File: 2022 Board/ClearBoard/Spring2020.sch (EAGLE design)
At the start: 20 parts, among them U1 TB67H401FTG(O,EL), U2 ABX00012, U3 V36SE05010NRFA

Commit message: Almost done with place and route
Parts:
- removed C1: ECA1CM101I, SnapEDA Library:ECA1CM101I
- removed U3: V36SE05010NRFA, SnapEDA Library:V36SE05010NRFA
- added PS1: NID100-5, SnapEDA Library:NID100-5
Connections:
- removed net BKGND: BIKE-PWR-1.KL, C15.2, C19.2, C3.2, GND-JUMPER.2, REAR-MOTOR.1, U$2.GND2, U$7.GND2, U1.GND_3, U3.-VIN
- removed net N$1: U3.-SENSE
- net 5V: now also PS1.+VOUT; no longer C1.P, U3.+SENSE, U3.+VOUT
- net BKPWR: now also PS1.+VIN; no longer U3.+VIN
- net GND: now also BIKE-PWR-1.KL, C15.2, C19.2, C3.2, GND-JUMPER.2, PS1.COM, REAR-MOTOR.1, U$2.GND2, U$7.GND2, U1.GND_3; no longer C1.N, U3.-VOUT
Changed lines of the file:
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@@
 <part name="U2" library="SnapEDA Library" deviceset="ABX00012" device=""/>
 <part name="PWM" library="rcl" library_urn="urn:adsk.eagle:library:334" deviceset="R-US_" device="0204/2V" package3d_urn="urn:adsk.eagle:package:23495/1" value="68000"/>
-<part name="U3" library="SnapEDA Library" deviceset="V36SE05010NRFA" device=""/>
-<part name="C1" library="SnapEDA Library" deviceset="ECA1CM101I" device=""/>
 <part name="U$3" library="Spring2016Optoisolator" deviceset="IL-711" device=""/>
 <part name="C2" library="resistor" deviceset="C-US" device="025-050X050"/>
@@
 <part name="U$2" library="Spring2016Optoisolator" deviceset="IL-712" device=""/>
 <part name="U1" library="Test" deviceset="TB67H401FTG(O,EL)" device=""/>
+<part name="PS1" library="SnapEDA Library" deviceset="NID100-5" device=""/>
 </parts>
 <sheets>
@@
 <attribute name="VALUE" x="166.37" y="155.702" size="1.778" layer="96" rot="R180"/>
 </instance>
-<instance part="U3" gate="G$1" x="294.64" y="147.32" smashed="yes">
-<attribute name="NAME" x="281.94" y="158.75" size="1.778" layer="95"/>
-<attribute name="VALUE" x="281.94" y="134.62" size="1.778" layer="96"/>
-</instance>
-<instance part="C1" gate="G$1" x="325.12" y="157.48" smashed="yes" rot="R270">
-<attribute name="NAME" x="328.93" y="160.02" size="1.778" layer="95" rot="R270"/>
-<attribute name="VALUE" x="320.04" y="160.02" size="1.778" layer="96" rot="R270"/>
-</instance>
 <instance part="U$3" gate="G$1" x="337.82" y="45.72" smashed="yes" rot="R180"/>
 <instance part="C2" gate="G$1" x="88.9" y="124.46" smashed="yes" rot="R270">
@@
 <attribute name="NAME" x="188.3156" y="98.0186" size="2.0828" layer="95" ratio="6" rot="SR0"/>
 <attribute name="VALUE" x="187.6806" y="95.4786" size="2.0828" layer="96" ratio="6" rot="SR0"/>
+</instance>
+<instance part="PS1" gate="G$1" x="294.64" y="177.8" smashed="yes">
+<attribute name="NAME" x="279.4" y="186.182" size="1.778" layer="95"/>
+<attribute name="VALUE" x="279.4" y="167.64" size="1.778" layer="96"/>
 </instance>
 </instances>
@@
 </segment>
 <segment>
-<pinref part="C1" gate="G$1" pin="N"/>
-<pinref part="U3" gate="G$1" pin="-VOUT"/>
-<wire x1="325.12" y1="152.4" x2="312.42" y2="152.4" width="0.1524" layer="91"/>
-<label x="312.42" y="152.4" size="1.778" layer="95"/>
-</segment>
-<segment>
 <wire x1="93.98" y1="109.22" x2="83.82" y2="109.22" width="0.1524" layer="91"/>
 <label x="93.98" y="109.22" size="1.778" layer="95" rot="R180"/>
@@
 <wire x1="83.82" y1="124.46" x2="78.74" y2="124.46" width="0.1524" layer="91"/>
 <label x="78.74" y="124.46" size="1.778" layer="95"/>
+</segment>
+<segment>
+<pinref part="PS1" gate="G$1" pin="COM"/>
+<wire x1="314.96" y1="172.72" x2="325.12" y2="172.72" width="0.1524" layer="91"/>
+<label x="317.5" y="172.72" size="1.778" layer="95"/>
+</segment>
+<segment>
+<pinref part="BIKE-PWR" gate="-1" pin="KL"/>
+<wire x1="294.64" y1="48.26" x2="292.1" y2="48.26" width="0.1524" layer="91"/>
+<label x="294.64" y="48.26" size="1.778" layer="95"/>
+</segment>
+<segment>
+<pinref part="GND-JUMPER" gate="A" pin="2"/>
+<wire x1="289.56" y1="25.4" x2="294.64" y2="25.4" width="0.1524" layer="91"/>
+<label x="292.1" y="25.4" size="1.778" layer="95"/>
+</segment>
+<segment>
+<wire x1="170.18" y1="53.34" x2="160.02" y2="53.34" width="0.1524" layer="91"/>
+<label x="160.02" y="53.34" size="1.778" layer="95"/>
+<pinref part="U1" gate="A" pin="GND_3"/>
+</segment>
+<segment>
+<pinref part="REAR-MOTOR" gate="1" pin="1"/>
+<wire x1="195.58" y1="154.94" x2="187.96" y2="154.94" width="0.1524" layer="91"/>
+<label x="195.58" y="154.94" size="1.778" layer="95" rot="R180"/>
+</segment>
+<segment>
+<wire x1="129.54" y1="142.24" x2="134.62" y2="142.24" width="0.1524" layer="91"/>
+<label x="129.54" y="142.24" size="1.778" layer="95"/>
+<pinref part="U$7" gate="G$1" pin="GND2"/>
+</segment>
+<segment>
+<pinref part="C19" gate="G$1" pin="2"/>
+<wire x1="147.32" y1="157.48" x2="149.86" y2="157.48" width="0.1524" layer="91"/>
+<label x="147.32" y="157.48" size="1.778" layer="95"/>
+</segment>
+<segment>
+<pinref part="C15" gate="G$1" pin="2"/>
+<wire x1="167.64" y1="142.24" x2="167.64" y2="139.7" width="0.1524" layer="91"/>
+<label x="167.64" y="142.24" size="1.778" layer="95"/>
+</segment>
+<segment>
+<wire x1="127" y1="109.22" x2="132.08" y2="109.22" width="0.1524" layer="91"/>
+<label x="127" y="109.22" size="1.778" layer="95"/>
+<pinref part="U$2" gate="G$1" pin="GND2"/>
+</segment>
+<segment>
+<pinref part="C3" gate="G$1" pin="2"/>
+<wire x1="144.78" y1="124.46" x2="149.86" y2="124.46" width="0.1524" layer="91"/>
+<label x="144.78" y="124.46" size="1.778" layer="95"/>
 </segment>
 </net>
@@
 </segment>
 </net>
-<net name="BKGND" class="0">
-<segment>
-<pinref part="BIKE-PWR" gate="-1" pin="KL"/>
-<wire x1="294.64" y1="48.26" x2="292.1" y2="48.26" width="0.1524" layer="91"/>
-<label x="294.64" y="48.26" size="1.778" layer="95"/>
-</segment>
-<segment>
-<pinref part="GND-JUMPER" gate="A" pin="2"/>
-<wire x1="289.56" y1="25.4" x2="294.64" y2="25.4" width="0.1524" layer="91"/>
-<label x="292.1" y="25.4" size="1.778" layer="95"/>
-</segment>
-<segment>
-<wire x1="170.18" y1="53.34" x2="160.02" y2="53.34" width="0.1524" layer="91"/>
-<label x="160.02" y="53.34" size="1.778" layer="95"/>
-<pinref part="U1" gate="A" pin="GND_3"/>
-</segment>
-<segment>
-<pinref part="REAR-MOTOR" gate="1" pin="1"/>
-<wire x1="195.58" y1="154.94" x2="187.96" y2="154.94" width="0.1524" layer="91"/>
-<label x="195.58" y="154.94" size="1.778" layer="95" rot="R180"/>
-</segment>
-<segment>
-<wire x1="129.54" y1="142.24" x2="134.62" y2="142.24" width="0.1524" layer="91"/>
-<label x="129.54" y="142.24" size="1.778" layer="95"/>
-<pinref part="U$7" gate="G$1" pin="GND2"/>
-</segment>
-<segment>
-<pinref part="C19" gate="G$1" pin="2"/>
-<wire x1="147.32" y1="157.48" x2="149.86" y2="157.48" width="0.1524" layer="91"/>
-<label x="147.32" y="157.48" size="1.778" layer="95"/>
-</segment>
-<segment>
-<pinref part="C15" gate="G$1" pin="2"/>
-<wire x1="167.64" y1="142.24" x2="167.64" y2="139.7" width="0.1524" layer="91"/>
-<label x="167.64" y="142.24" size="1.778" layer="95"/>
-</segment>
-<segment>
-<pinref part="U3" gate="G$1" pin="-VIN"/>
-<wire x1="266.7" y1="152.4" x2="276.86" y2="152.4" width="0.1524" layer="91"/>
-<label x="266.7" y="152.4" size="1.778" layer="95"/>
-</segment>
-<segment>
-<wire x1="127" y1="109.22" x2="132.08" y2="109.22" width="0.1524" layer="91"/>
-<label x="127" y="109.22" size="1.778" layer="95"/>
-<pinref part="U$2" gate="G$1" pin="GND2"/>
-</segment>
-<segment>
-<pinref part="C3" gate="G$1" pin="2"/>
-<wire x1="144.78" y1="124.46" x2="149.86" y2="124.46" width="0.1524" layer="91"/>
-<label x="144.78" y="124.46" size="1.778" layer="95"/>
-</segment>
-</net>
 <net name="CH5" class="0">
 <segment>
@@
 </segment>
 <segment>
-<pinref part="U3" gate="G$1" pin="+SENSE"/>
-<wire x1="274.32" y1="147.32" x2="276.86" y2="147.32" width="0.1524" layer="91"/>
-<label x="274.32" y="147.32" size="1.778" layer="95"/>
-</segment>
-<segment>
-<pinref part="U3" gate="G$1" pin="+VOUT"/>
-<wire x1="312.42" y1="154.94" x2="317.5" y2="154.94" width="0.1524" layer="91"/>
-<label x="312.42" y="154.94" size="1.778" layer="95"/>
-<wire x1="317.5" y1="154.94" x2="317.5" y2="160.02" width="0.1524" layer="91"/>
-<pinref part="C1" gate="G$1" pin="P"/>
-<wire x1="317.5" y1="160.02" x2="325.12" y2="160.02" width="0.1524" layer="91"/>
-</segment>
-<segment>
 <label x="129.54" y="124.46" size="1.778" layer="95"/>
 <wire x1="127" y1="124.46" x2="137.16" y2="124.46" width="0.1524" layer="91"/>
@@
 <pinref part="U$2" gate="G$1" pin="VDD2"/>
 </segment>
+<segment>
+<pinref part="PS1" gate="G$1" pin="+VOUT"/>
+<wire x1="314.96" y1="182.88" x2="325.12" y2="182.88" width="0.1524" layer="91"/>
+<label x="317.5" y="182.88" size="1.778" layer="95"/>
+</segment>
 </net>
 <net name="BKPWR" class="0">
@@
 </segment>
 <segment>
-<pinref part="U3" gate="G$1" pin="+VIN"/>
-<label x="266.7" y="154.94" size="1.778" layer="95"/>
-<wire x1="276.86" y1="154.94" x2="266.7" y2="154.94" width="0.1524" layer="91"/>
+<wire x1="274.32" y1="182.88" x2="264.16" y2="182.88" width="0.1524" layer="91"/>
+<pinref part="PS1" gate="G$1" pin="+VIN"/>
+<label x="264.16" y="182.88" size="1.778" layer="95"/>
 </segment>
 </net>
@@
 </segment>
 </net>
-<net name="N$1" class="0">
-<segment>
-<pinref part="U3" gate="G$1" pin="-SENSE"/>
-<wire x1="276.86" y1="144.78" x2="271.78" y2="144.78" width="0.1524" layer="91"/>
-</segment>
-</net>

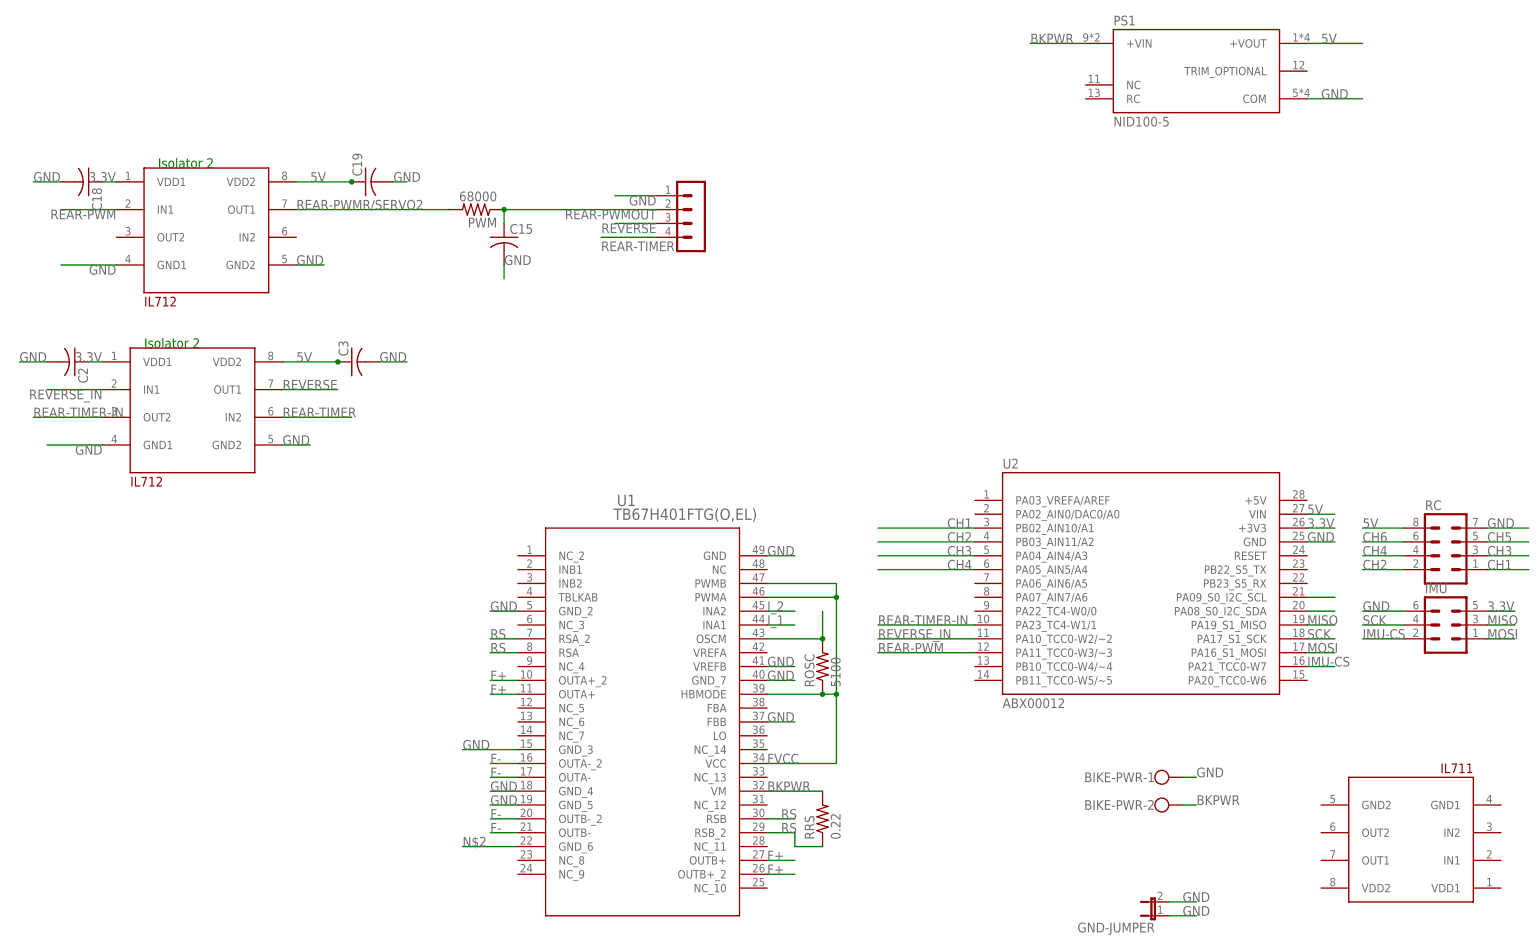
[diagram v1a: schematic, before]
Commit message: Finished front motor attachments
Also positioned things in board
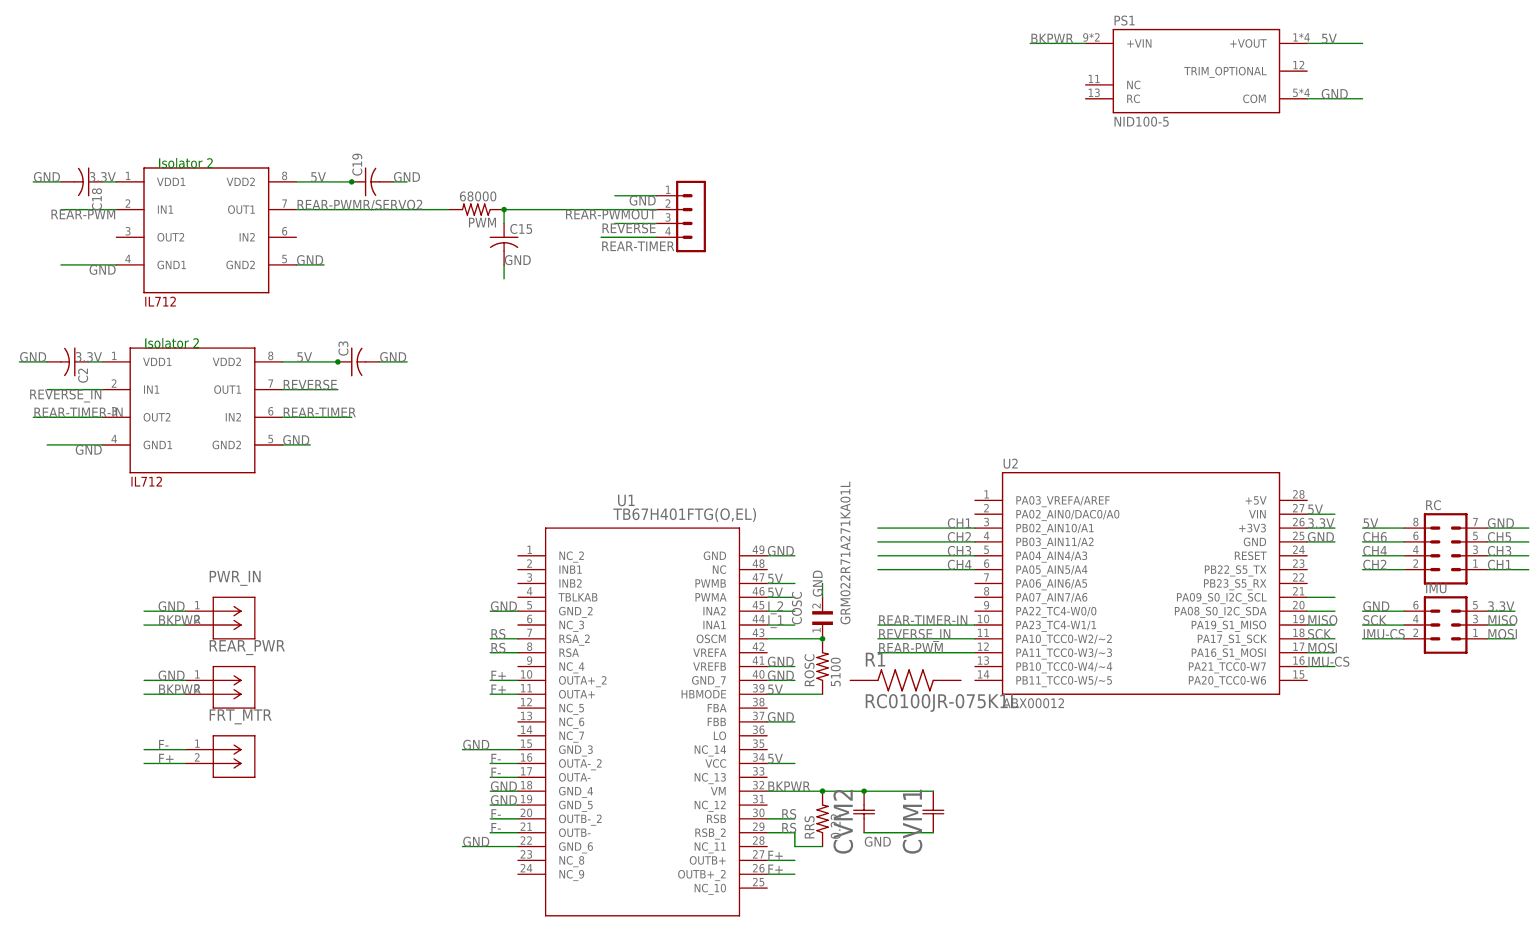
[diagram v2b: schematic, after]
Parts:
- removed BIKE-PWR: (no value), con-wago-500:W237-102
- removed GND-JUMPER: (no value), jumper:JP1E
- removed U$3: IL-711, Spring2016Optoisolator:IL-711
- added COSC: GRM022R71A271KA01L, SnapEDA Library:GRM022R71A271KA01L
- added CVM1: 860010674014, Test:860010674014
- added CVM2: CL05B104KB54PNC, Test:CL05B104KB54PNC
- added FRT_MTR, PWR_IN, REAR_PWR: 1792863, Test:1792863
- added R1: RC0100JR-075K1L, SnapEDA Library:RC0100JR-075K1L
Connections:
- removed net FVCC: ROSC.1, U1.HBMODE, U1.PWMA, U1.PWMB, U1.VCC
- removed net N$2: U1.GND_6
- net 5V: now also ROSC.1, U1.HBMODE, U1.PWMA, U1.PWMB, U1.VCC
- net BKPWR: now also CVM1.2, CVM2.2, PWR_IN.2, REAR_PWR.2; no longer BIKE-PWR-2.KL
- net F+: now also FRT_MTR.2
- net F-: now also FRT_MTR.1
- net GND: now also COSC.2, CVM1.1, CVM2.1, PWR_IN.1, REAR_PWR.1, U1.GND_6; no longer BIKE-PWR-1.KL, GND-JUMPER.1, GND-JUMPER.2
- net N$5: now also COSC.1
